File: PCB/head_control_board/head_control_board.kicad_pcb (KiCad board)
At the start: 2 copper layers, 0 parts

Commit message: Finish first pass of schematic
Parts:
- added BOOT1: TS-1187A-B-A-B, LCSC:SW-SMD_4P-L5.1-W5.1-P3.70-LS6.5-TL-2, F.Cu at (178.4, 115.0)
- added C1: 10uF 0805, Capacitor_SMD:C_0805_2012Metric, F.Cu at (216.3, 99.7)
- added C10: 100nF, Capacitor_SMD:C_0402_1005Metric, F.Cu at (228.8, 101.2)
- added C11: 22uF 0805, Capacitor_SMD:C_0805_2012Metric, F.Cu at (220.7, 99.7)
- added C12: 22uF 0805, Capacitor_SMD:C_0805_2012Metric, F.Cu at (220.7, 102.7)
- added C13: 22uF 0805, Capacitor_SMD:C_0805_2012Metric, F.Cu at (220.7, 105.8)
- added C14: 22uF 0805, Capacitor_SMD:C_0805_2012Metric, F.Cu at (220.7, 108.8)
- added C15: 10uF, Capacitor_SMD:C_0805_2012Metric, F.Cu at (225.2, 99.7)
- added C16: 22uF 0805, Capacitor_SMD:C_0805_2012Metric, F.Cu at (225.2, 102.7)
- added C17: 22uF 0805, Capacitor_SMD:C_0805_2012Metric, F.Cu at (225.2, 105.8)
- added C18: 10uF, Capacitor_SMD:C_0805_2012Metric, F.Cu at (225.2, 108.8)
- added C19: 0.1uF, Capacitor_SMD:C_0603_1608Metric, F.Cu at (197.2, 123.1)
- added C2: 10uF 0805, Capacitor_SMD:C_0805_2012Metric, F.Cu at (216.3, 102.7)
- added C20: 0.1uF, Capacitor_SMD:C_0603_1608Metric, F.Cu at (201.2, 113.0)
- added C21: 0.1uF, Capacitor_SMD:C_0603_1608Metric, F.Cu at (201.2, 115.5)
- added C22: 100nF, Capacitor_SMD:C_0402_1005Metric, F.Cu at (228.8, 103.2)
- added C3: 10uF 0805, Capacitor_SMD:C_0805_2012Metric, F.Cu at (216.3, 105.8)
- added C4: 10uF 0805, Capacitor_SMD:C_0805_2012Metric, F.Cu at (216.3, 108.8)
- added C5: 10uF 0603, Capacitor_SMD:C_0603_1608Metric, F.Cu at (197.2, 113.0)
- added C6: 10uF 0603, Capacitor_SMD:C_0603_1608Metric, F.Cu at (197.2, 115.5)
- added C7: 10uF 0603, Capacitor_SMD:C_0603_1608Metric, F.Cu at (197.2, 118.0)
- added C8: 10uF 0603, Capacitor_SMD:C_0603_1608Metric, F.Cu at (197.2, 120.6)
- added C9: 100nF, Capacitor_SMD:C_0402_1005Metric, F.Cu at (228.8, 99.2)
- added COIL1: JST-XH 2P, Connector_JST:JST_XH_S2B-XH-A-1_1x02_P2.50mm_Horizontal, F.Cu at (198.6, 103.2)
- added D1: D, LCSC:SMA_L4.3-W2.6-LS5.2-RD, F.Cu at (210.9, 113.8)
- added D2: D, LCSC:SMA_L4.3-W2.6-LS5.2-RD, F.Cu at (210.9, 117.8)
- added D3: D, LCSC:SMA_L4.3-W2.6-LS5.2-RD, F.Cu at (210.9, 121.8)
- added D4: D, LCSC:SMA_L4.3-W2.6-LS5.2-RD, F.Cu at (210.9, 125.8)
- added D5: D, LCSC:SMA_L4.3-W2.6-LS5.2-RD, F.Cu at (119.0, 120.0)
- added D6: IP4234CZ6,125, LCSC:SOT-457_L2.9-W1.5-P0.95-LS2.8-BL, F.Cu at (127.7, 127.0)
- added H1: MountingHole_Pad, MountingHole:MountingHole_2.5mm_Pad_Via, F.Cu at (190.7, 115.1)
- added H2: MountingHole_Pad, MountingHole:MountingHole_2.5mm_Pad_Via, F.Cu at (190.7, 121.7)
- added HOLO1: JST-XH 3P, Connector_JST:JST_XH_S3B-XH-A-1_1x03_P2.50mm_Horizontal, F.Cu at (198.6, 89.6)
- added L1: 1.5uH, LCSC:IND-SMD_L7.0-W6.6, F.Cu at (219.3, 115.7)
- added L2: 1.5uH, LCSC:IND-SMD_L7.0-W6.6, F.Cu at (219.3, 123.5)
- added LED1: WS2812B-MINI, LCSC:LED-SMD_4P-L3.5-W3.5-TL_WS2812B, F.Cu at (191.2, 127.3)
- added LOGIC1: JST-XH 3P, Connector_JST:JST_XH_S3B-XH-A-1_1x03_P2.50mm_Horizontal, F.Cu at (210.6, 89.6)
- added PSI1: JST-XH 3P, Connector_JST:JST_XH_S3B-XH-A-1_1x03_P2.50mm_Horizontal, F.Cu at (222.5, 89.6)
- added R1: 5.1k, Resistor_SMD:R_0805_2012Metric, F.Cu at (129.1, 114.0)
- added R10: 100k, Resistor_SMD:R_0603_1608Metric, F.Cu at (205.2, 118.0)
- added R11: 10k, Resistor_SMD:R_0805_2012Metric, F.Cu at (185.2, 125.1)
- added R12: 60, Resistor_SMD:R_0805_2012Metric, F.Cu at (185.2, 128.1)
- added R13: 10k, Resistor_SMD:R_0805_2012Metric, F.Cu at (185.2, 131.0)
- added R2: 5.1k, Resistor_SMD:R_0805_2012Metric, F.Cu at (135.1, 117.0)
- added R3: 10k, Resistor_SMD:R_0805_2012Metric, F.Cu at (185.2, 119.2)
- added R4: 10k, Resistor_SMD:R_0805_2012Metric, F.Cu at (185.2, 122.2)
- added R5: 680k, Resistor_SMD:R_0603_1608Metric, F.Cu at (201.2, 118.0)
- added R6: 470k, Resistor_SMD:R_0603_1608Metric, F.Cu at (201.2, 120.6)
- added R7: 130k, Resistor_SMD:R_0603_1608Metric, F.Cu at (201.2, 123.1)
- added R8: 150k, Resistor_SMD:R_0603_1608Metric, F.Cu at (205.2, 113.0)
- added R9: 100k, Resistor_SMD:R_0603_1608Metric, F.Cu at (205.2, 115.5)
- added RADAR1: JST-XH 2P, Connector_JST:JST_XH_S2B-XH-A-1_1x02_P2.50mm_Horizontal, F.Cu at (208.1, 103.2)
- added RESET1: TS-1187A-B-A-B, LCSC:SW-SMD_4P-L5.1-W5.1-P3.70-LS6.5-TL-2, F.Cu at (178.4, 121.3)
- added TP1: TestPoint, TestPoint:TestPoint_Pad_D2.0mm, F.Cu at (226.0, 123.0)
- added TP2: TestPoint, TestPoint:TestPoint_Pad_D2.0mm, F.Cu at (226.0, 127.0)
- added U1: TYPE-C 14PLC-H10.0, LCSC:USB-C-TH_SHOUHAN_TYPE-C-14PLC-H10.0, F.Cu at (127.8, 133.7)
- added U2: TPS63070RNMR, LCSC:VQFN-HR-15_L3.0-W2.5-P0.50-BL_TPS63070RNMR, F.Cu at (226.3, 114.0)
- added U3: TPS63070RNMR, LCSC:VQFN-HR-15_L3.0-W2.5-P0.50-BL_TPS63070RNMR, F.Cu at (226.3, 118.6)
- added U4: SN74AHCT245PWR, LCSC:TSSOP-20_L6.5-W4.4-P0.65-LS6.4-BL, F.Cu at (178.1, 128.8)
- added U5: ESP32-S3-WROOM-1(N16R8), LCSC:WIRELM-SMD_ESP32-S3-WROOM-1, F.Cu at (121.1, 99.9)

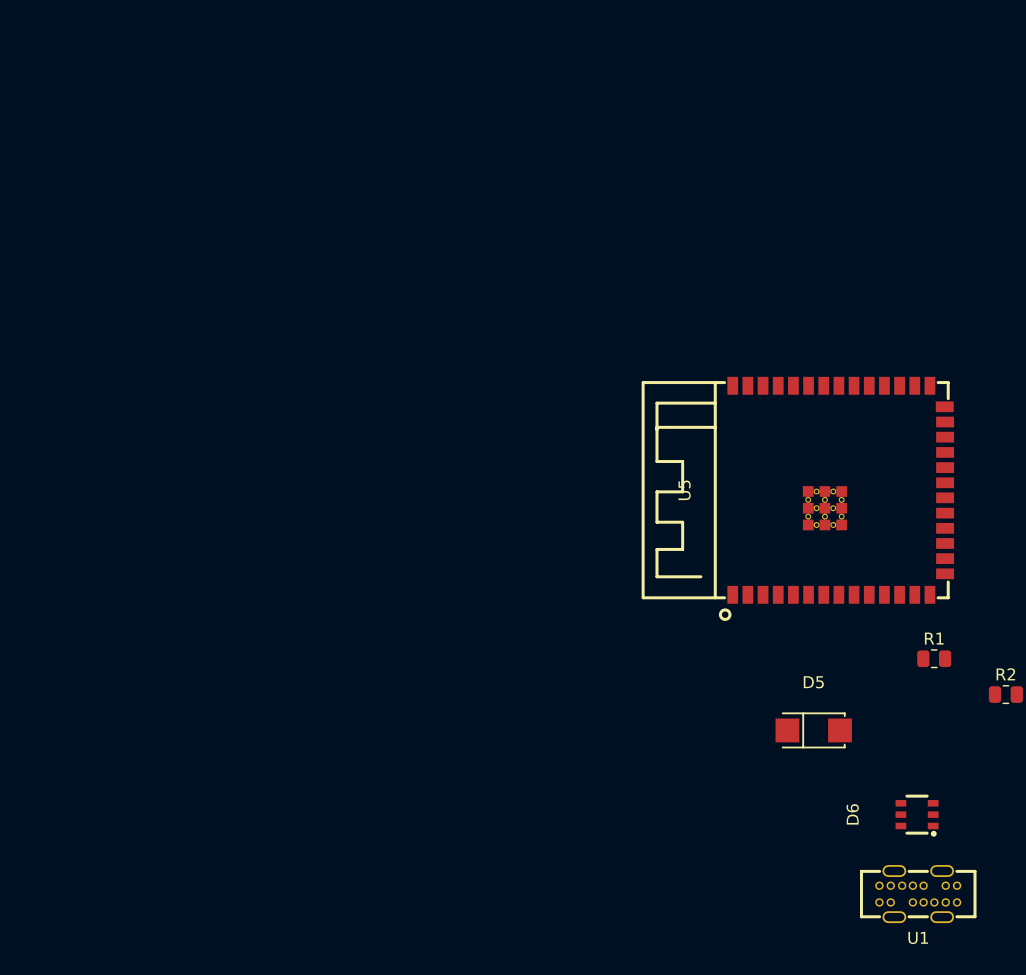
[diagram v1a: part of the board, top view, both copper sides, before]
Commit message: Add connector pin labels
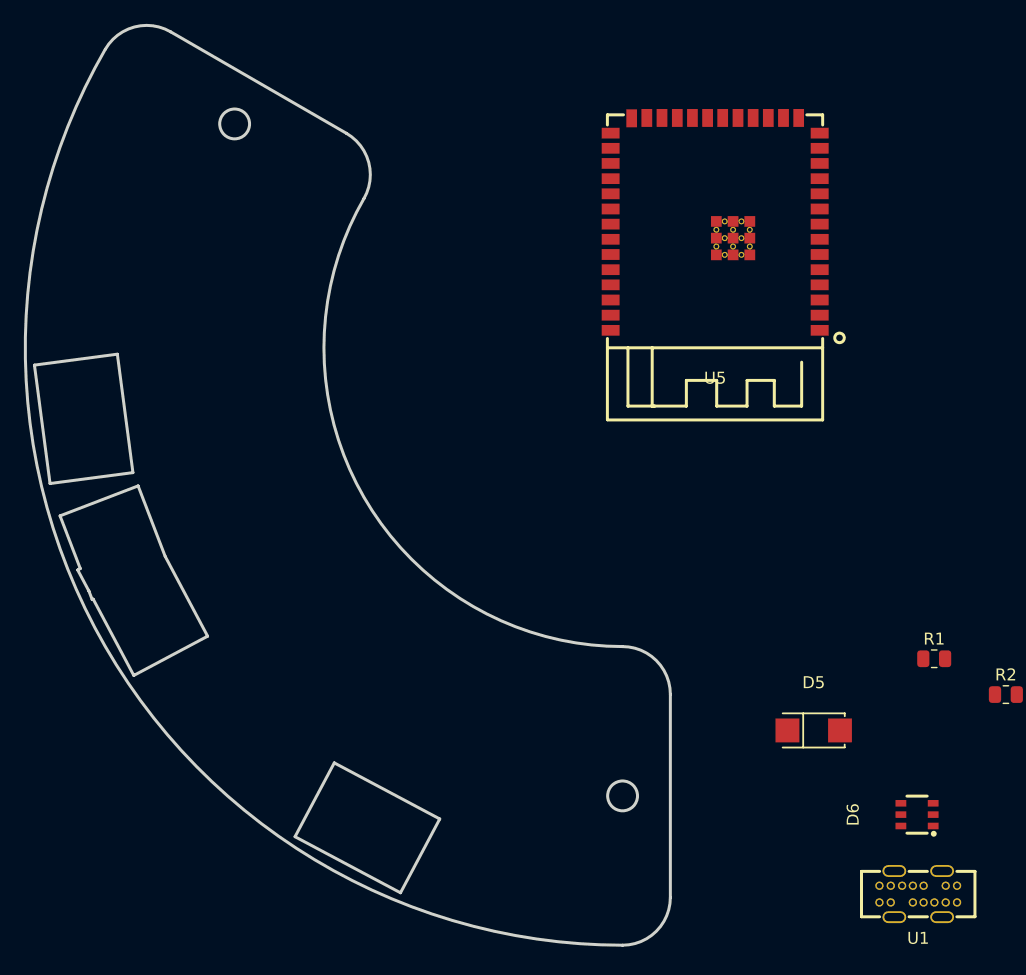
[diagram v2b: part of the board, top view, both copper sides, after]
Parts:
- moved U5 24.6 mm to (110.8, 77.6), turned to 180 degrees
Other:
- board outline added: 54 x 77 mm
- board text added: "For Instructional Use Only."
- board text added: "SOLIDWORKS Educational Product."

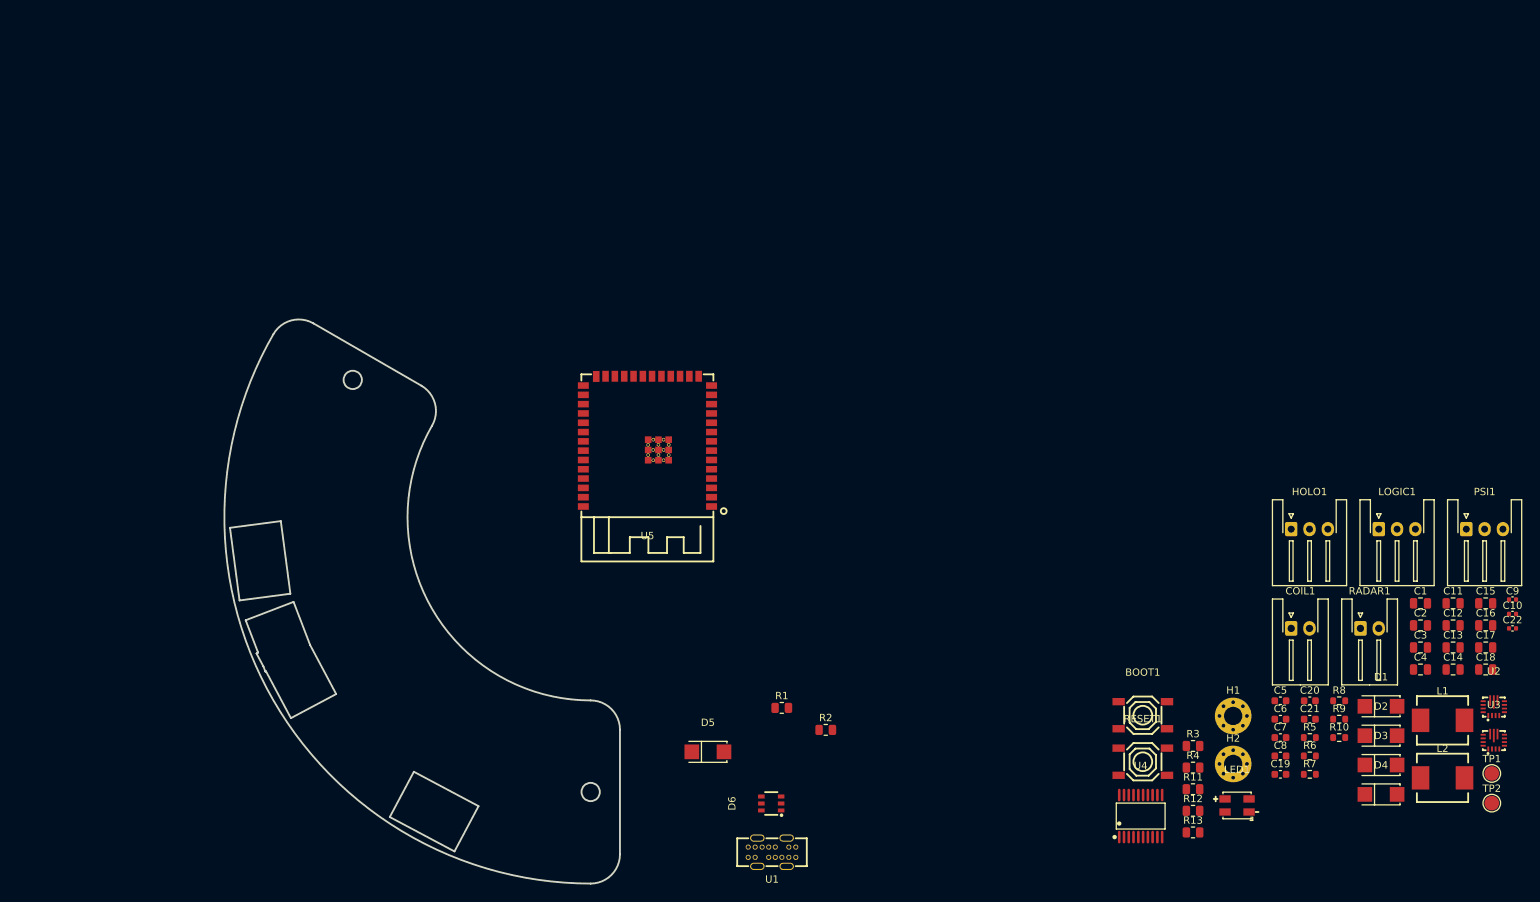
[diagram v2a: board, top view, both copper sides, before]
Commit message: Update schematic and route usb
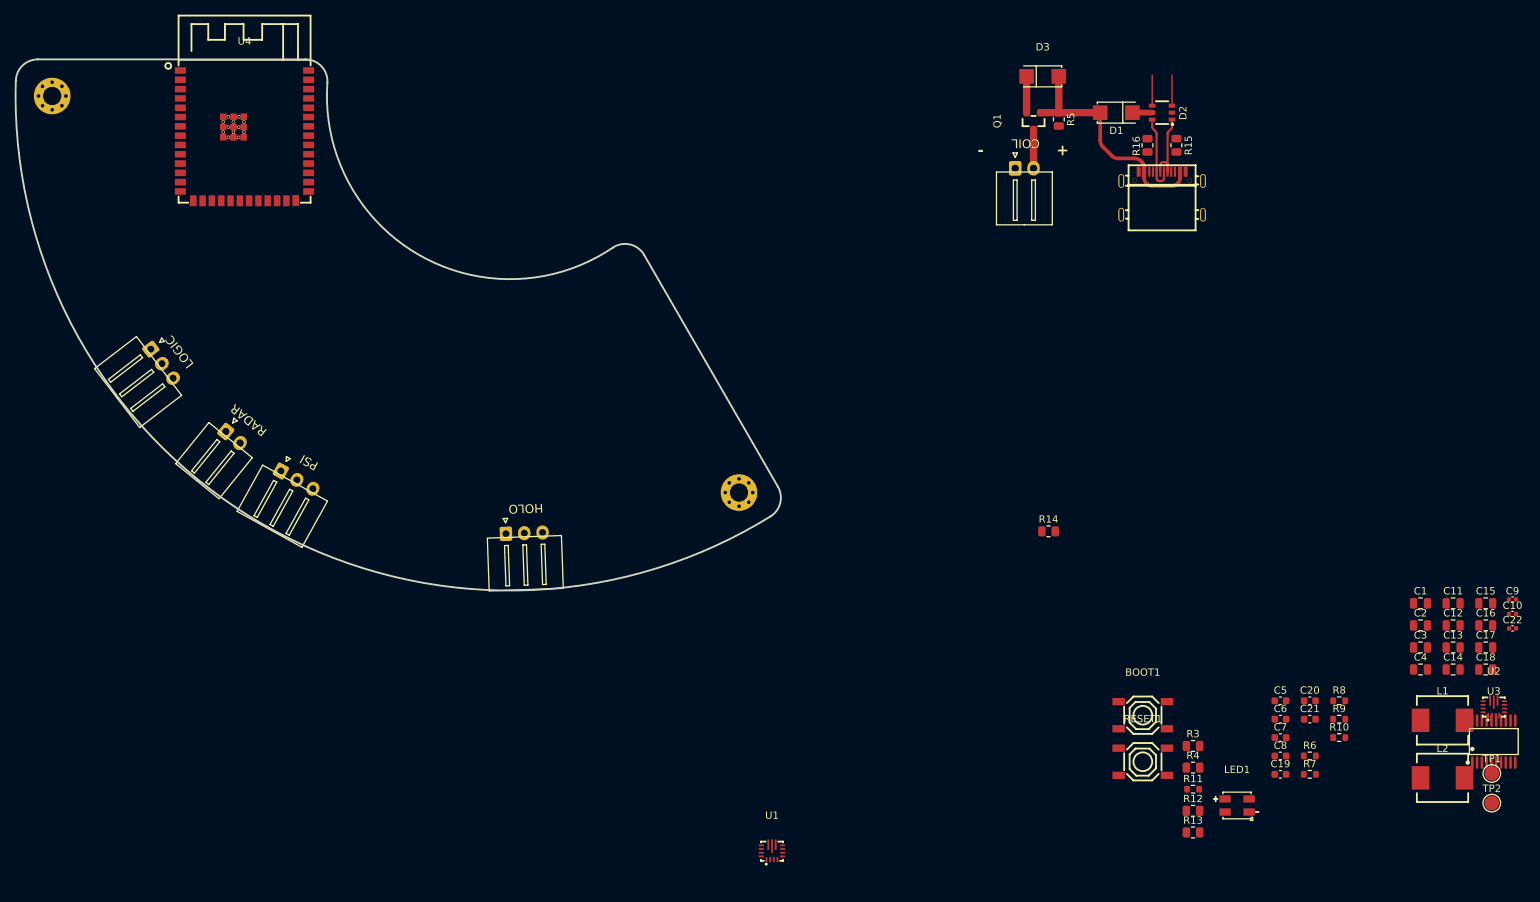
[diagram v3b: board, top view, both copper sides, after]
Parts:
- removed D4, D5: D, LCSC:SMA_L4.3-W2.6-LS5.2-RD
- removed D6: IP4234CZ6,125, LCSC:SOT-457_L2.9-W1.5-P0.95-LS2.8-BL
- removed R1, R2: 5.1k, Resistor_SMD:R_0805_2012Metric
- removed U5: ESP32-S3-WROOM-1(N16R8), LCSC:WIRELM-SMD_ESP32-S3-WROOM-1
- added Q1: AO3401A, LCSC:SOT-23_L2.9-W1.3-P1.90-LS2.4-BR, F.Cu at (163.4, 33.9)
- added R14: 10k, Resistor_SMD:R_0805_2012Metric, F.Cu at (165.5, 89.9)
- added R15: 5.1k, Resistor_SMD:R_0805_2012Metric, F.Cu at (182.9, 37.2)
- added R16: 5.1k, Resistor_SMD:R_0805_2012Metric, F.Cu at (179.0, 37.2)
- added USBC1: TYPE-C-31-M-14, LCSC:USB-C-SMD_12P-P0.50-H-F_TYPE-C-31-M-14, F.Cu at (181.0, 43.7)
- C15: value 10uF -> 22uF 0805
- C17: value 22uF 0805 -> 10uF
- D2: value D -> IP4234CZ6; footprint LCSC:SMA_L4.3-W2.6-LS5.2-RD -> LCSC:SOT-457_L2.9-W1.5-P0.95-LS2.8-BL
- R11: value 10k -> 100k; footprint Resistor_SMD:R_0805_2012Metric -> Resistor_SMD:R_0603_1608Metric
- R12: value 60 -> 10k
- R13: value 10k -> 60
- R5: value 680k -> 100k; footprint Resistor_SMD:R_0603_1608Metric -> Resistor_SMD:R_0805_2012Metric
- R6: value 470k -> 680k
- R7: value 130k -> 470k
- R8: value 150k -> 130k
- R9: value 100k -> 150k
- U1: value TYPE-C 14PLC-H10.0 -> TPS63070RNMR; footprint LCSC:USB-C-TH_SHOUHAN_TYPE-C-14PLC-H10.0 -> LCSC:VQFN-HR-15_L3.0-W2.5-P0.50-BL_TPS63070RNMR
- U3: value TPS63070RNMR -> SN74AHCT245PWR; footprint LCSC:VQFN-HR-15_L3.0-W2.5-P0.50-BL_TPS63070RNMR -> LCSC:TSSOP-20_L6.5-W4.4-P0.65-LS6.4-BL
- U4: value SN74AHCT245PWR -> ESP32-S3-WROOM-1(N16R8); footprint LCSC:TSSOP-20_L6.5-W4.4-P0.65-LS6.4-BL -> LCSC:WIRELM-SMD_ESP32-S3-WROOM-1
- moved H1 182.1 mm to (29.5, 30.5)
- moved LOGIC1 169.4 mm to (43.0, 65.0), turned to -52.5 degrees
- moved PSI1 162.0 mm to (60.7, 81.7), turned to -29 degrees
- moved RADAR1 157.2 mm to (53.2, 76.3), turned to -39 degrees
- moved U4 153.6 mm to (55.8, 35.9)
- moved HOLO1 107.2 mm to (91.4, 90.2), turned to 2 degrees
- moved D3 104.7 mm to (164.7, 27.8)
- moved R5 91.1 mm to (166.9, 33.7), turned to -90 degrees
- moved D2 90.1 mm to (181.0, 32.8), turned to 90 degrees
- moved D1 88.7 mm to (174.8, 32.8), turned to 180 degrees
- moved H2 77.0 mm to (123.2, 84.6)
- moved COIL1 73.2 mm to (160.9, 40.4)
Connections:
- C1 pad 2: Net-(C1-Pad2) -> +VIN
- C10 pad 1: Net-(U3-Vaux) -> Net-(U2-Vaux)
- C16 pad 2: +5V -> +3.3V
- C17 pad 2: +3.3V -> +5V
- C2 pad 2: Net-(C2-Pad2) -> +VIN
- C3 pad 2: Net-(C1-Pad2) -> +VIN
- C4 pad 2: Net-(C2-Pad2) -> +VIN
- C5 pad 2: Net-(C1-Pad2) -> +VIN
- C6 pad 2: Net-(C2-Pad2) -> +VIN
- C9 pad 1: Net-(U2-Vaux) -> Net-(U1-Vaux)
- COIL1 pad 1: +VCOIL -> GND
- COIL1 pad 2: GND -> +VCOIL
- D1 pad 1: Net-(C1-Pad2) -> Net-(D1-Pad1)
- D1 pad 2: +VCOIL -> Net-(Q1-G)
- D2 pad 1: Net-(C2-Pad2) -> /D+
- D2 pad 2: +VCOIL -> GND
- D3 pad 1: Net-(C1-Pad2) -> +VIN
- D3 pad 2: +VUSB -> Net-(Q1-G)
- HOLO1 pad 1: +5V -> GND
- HOLO1 pad 3: GND -> +5V
- L1 pad 1: Net-(U2-L1) -> Net-(U1-L1)
- L1 pad 2: Net-(U2-L2) -> Net-(U1-L2)
- L2 pad 1: Net-(U3-L1) -> Net-(U2-L1)
- L2 pad 2: Net-(U3-L2) -> Net-(U2-L2)
- LED1 pad 1: GND -> +3.3V
- LED1 pad 3: +3.3V -> GND
- LOGIC1 pad 1: +5V -> GND
- LOGIC1 pad 3: GND -> +5V
- PSI1 pad 1: +5V -> GND
- PSI1 pad 3: GND -> +5V
- R10 pad 1: +3.3V -> +5V
- R10 pad 2: Net-(U3-PG) -> Net-(U1-PG)
- R11 pad 2: Net-(RESET1-A) -> Net-(U2-PG)
- R12 pad 2: Net-(RADAR1-Pin_1) -> Net-(RESET1-A)
- R13 pad 1: Net-(BOOT1-B) -> +3.3V
- R13 pad 2: +3.3V -> Net-(RADAR1-Pin_2)
- R3 pad 1: Net-(C1-Pad2) -> +VIN
- R3 pad 2: Net-(U2-EN) -> Net-(U1-EN)
- R4 pad 1: Net-(C2-Pad2) -> +VIN
- R4 pad 2: Net-(U3-EN) -> Net-(U2-EN)
- R5 pad 1: Net-(U2-FB) -> Net-(Q1-G)
- R5 pad 2: +5V -> GND
- R6 pad 1: Net-(U3-FB) -> Net-(U1-FB)
- R6 pad 2: +3.3V -> +5V
- R7 pad 1: GND -> Net-(U2-FB)
- R7 pad 2: Net-(U2-FB) -> +3.3V
- R8 pad 2: Net-(U3-FB) -> Net-(U1-FB)
- R9 pad 1: +5V -> GND
- R9 pad 2: Net-(U2-PG) -> Net-(U2-FB)
- RADAR1 pad 1: Net-(RADAR1-Pin_1) -> GND
- RADAR1 pad 2: GND -> Net-(RADAR1-Pin_2)
- U2 pad 12: Net-(C1-Pad2) -> +VIN
- U2 pad 13: Net-(C1-Pad2) -> +VIN
- U2 pad 7: +5V -> +3.3V
- U2 pad 8: +5V -> +3.3V
- U3 pad 1: Net-(U3-EN) -> +5V
- U3 pad 11: Net-(U3-L1) -> unconnected-(U3-B8-Pad11)
- U3 pad 12: Net-(C2-Pad2) -> unconnected-(U3-B7-Pad12)
- U3 pad 13: Net-(C2-Pad2) -> unconnected-(U3-B6-Pad13)
- U3 pad 14: Net-(U3-EN) -> unconnected-(U3-B5-Pad14)
- U3 pad 15: GND -> unconnected-(U3-B4-Pad15)
- U3 pad 2: Net-(U3-PG) -> /LED1_3V3
- U3 pad 3: Net-(U3-Vaux) -> /LED2_3V3
- U3 pad 4: GND -> /LED3_3V3
- U3 pad 5: Net-(U3-FB) -> unconnected-(U3-A4-Pad5)
- U3 pad 6: GND -> unconnected-(U3-A5-Pad6)
- U3 pad 7: +3.3V -> unconnected-(U3-A6-Pad7)
- U3 pad 8: +3.3V -> unconnected-(U3-A7-Pad8)
- U3 pad 9: Net-(U3-L2) -> unconnected-(U3-A8-Pad9)
- U4 pad 1: +5V -> GND
- U4 pad 10: GND -> unconnected-(U4-IO17-Pad10)
- U4 pad 13: unconnected-(U4-B6-Pad13) -> /USB-D-
- U4 pad 14: unconnected-(U4-B5-Pad14) -> /USB-D+
- U4 pad 16: /LED3_5V -> unconnected-(U4-IO46-Pad16)
- U4 pad 17: /LED2_5V -> unconnected-(U4-IO9-Pad17)
- U4 pad 18: /LED1_5V -> unconnected-(U4-IO10-Pad18)
- U4 pad 19: GND -> /LED1_3V3
- U4 pad 2: /LED1_3V3 -> +3.3V
- U4 pad 20: +5V -> /LED2_3V3
- U4 pad 3: /LED2_3V3 -> Net-(RESET1-B)
- U4 pad 4: /LED3_3V3 -> unconnected-(U4-IO4-Pad4)
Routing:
- net Net-(Q1-G): track 0.00 -> 33.2 mm
- net /D+: track 0.00 -> 10.5 mm
- net /D-: track 0.00 -> 10.5 mm
- net +VCOIL: track 0.00 -> 5.30 mm
- net +VIN: track 0.00 -> 4.95 mm
- net /USB-D-: track 0.00 -> 4.20 mm
- net /USB-D+: track 0.00 -> 4.20 mm
- net Net-(D1-Pad1): track 0.00 -> 2.70 mm
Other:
- board size 54 x 77 mm -> 104.5 x 72.5 mm
- board text added: "${REFERENCE}"
- board text added: "+"
- board text added: "-"
- board text added: "COIL"
- board text added: "HOLO"
- board text added: "LOGIC"
- board text added: "PSI"
- board text added: "RADAR"
- board text removed: "For Instructional Use Only."
- board text removed: "SOLIDWORKS Educational Product."
